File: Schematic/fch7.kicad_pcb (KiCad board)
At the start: 2 copper layers, 30 x 30 mm, 154 parts, among them IC1 MP9943AGQ-Z, IC2 MP9943AGQ-Z, IC3 STM32H743VIT6, IC4 ICM-42688-P, IC5 MPU-6500, J10 PIN2216, J11 PIN2216, J12 PIN2216, J2 PIN2216, J3 PIN2216, J4 PIN2216, J5 PIN2216, J6 PIN2216, J7 PIN2216, J8 PIN2216, J9 PIN2216, SW1 TS24CA, SW2 TS24CA, U1 ME6217C33M5G, U10 HDGC1002WR-S-4P, U11 HDGC1002WR-S-4P, U12 ESP-01F-2M, U13 E28-2G4M27SX, U14 HDGC1002WR-S-4P, U15 HDGC1002WR-S-6P, U16 HDGC1002WR-S-8P, U17 HDGC1002WR-S-8P, U2 ME6217C33M5G, U3 LDO-1.8v, U4 QMC5883L, U5 SPL06-001, U6 CSNP1GCR01-BOW, U7 HDGC1002WR-S-4P, U8 HDGC1002WR-S-4P, U9 HDGC1002WR-S-4P, Y1 8MHz

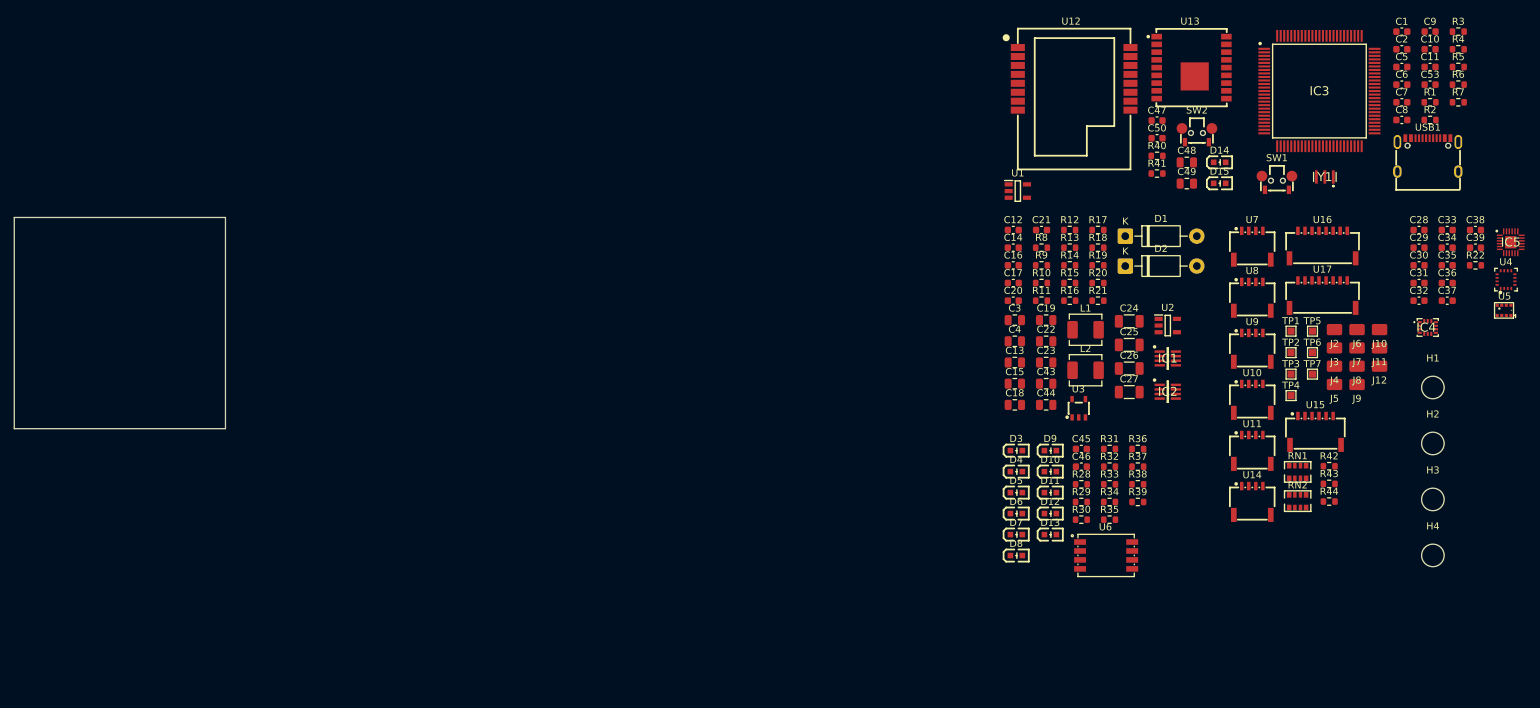
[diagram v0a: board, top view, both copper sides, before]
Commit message: Refactor mounting hole footprints and update schematic
- Deleted obsolete mounting hole footprints from the PCB design.
- Introduced a new footprint "MountingHole_quad_30.5x30.5" for improved layout.
- Updated references in the schematic to use the new mounting hole footprint.
- Adjusted positions of mounting hole symbols in the schematic for better alignment.
- Changed pin types for USB VBUS connections from "power_out" to "bidirectional" for accurate functionality.
- Cleaned up the footprint information cache to reflect the new footprint changes.
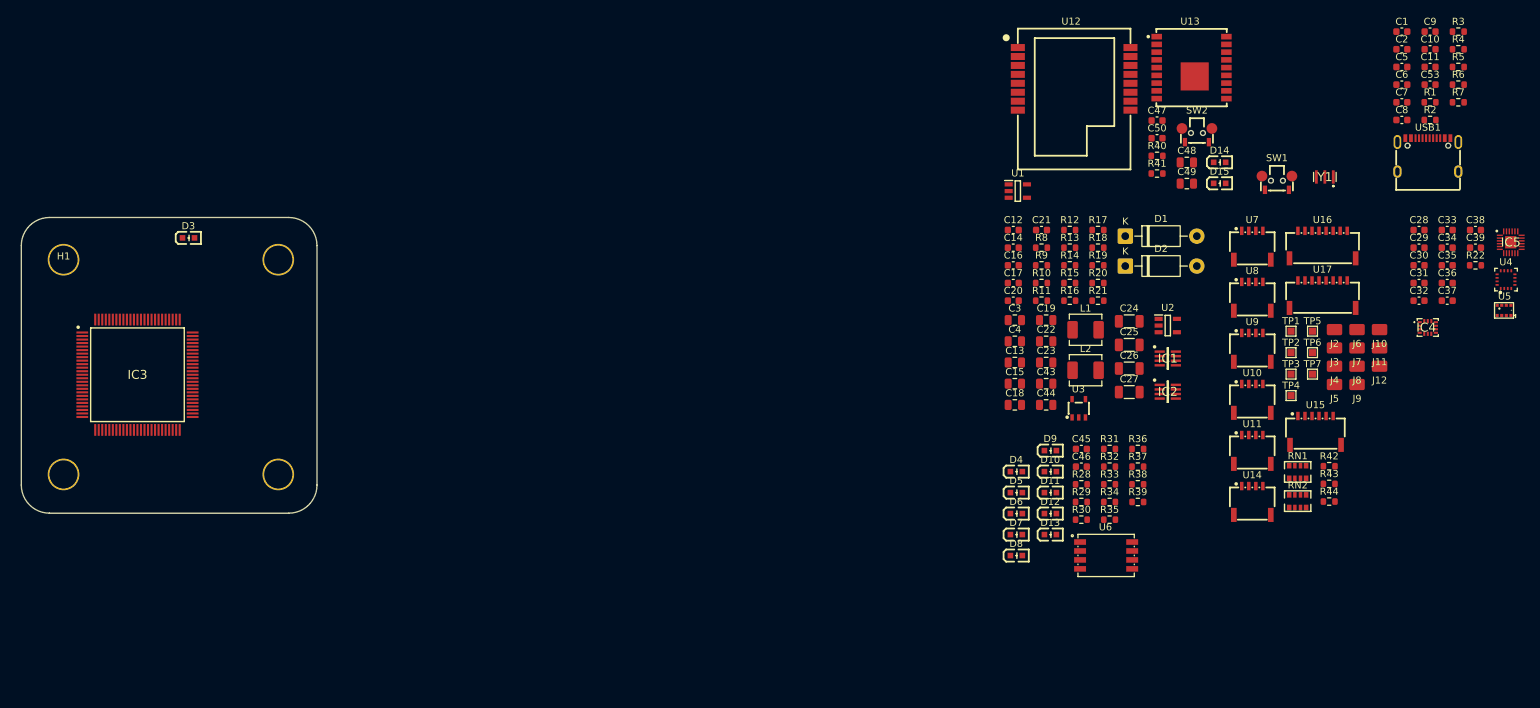
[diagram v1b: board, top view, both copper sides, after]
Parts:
- removed H2, H3, H4: MountingHole, MountingHole:MountingHole_3.2mm_M3
- H1: footprint MountingHole:MountingHole_3.2mm_M3 -> fch7_fp:MountingHole_quad_30.5x30.5
- moved H1 195.3 mm to (69.0, 66.0)
- moved IC3 172.7 mm to (79.5, 82.3)
- moved D3 121.4 mm to (86.8, 62.9)
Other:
- board size 30 x 30 mm -> 42 x 42 mm

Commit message: Update component properties for RF receiver schematic
- Changed the "Value" and "MPN" properties of components in the rf_rx.kicad_sch file from "E28-2G4M27SX" to "ESP-01F-2M".
- Reversed the previous changes for the same properties, updating them back to "E28-2G4M27SX".
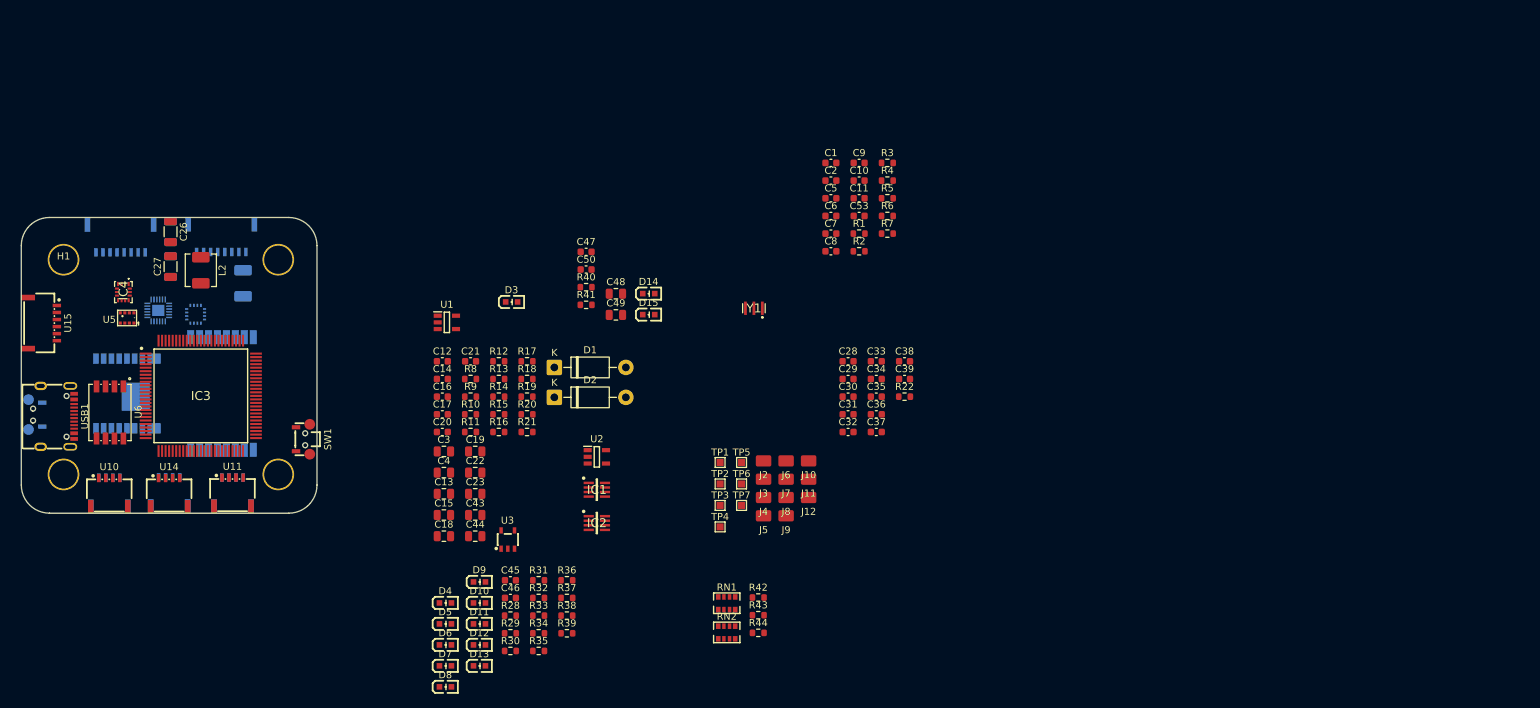
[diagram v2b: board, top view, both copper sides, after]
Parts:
- C24, C25, IC5, L1, SW2, U16, U17, U4, U7, U8, U9: moved to B.Cu
- U12: value ESP-01F-2M -> E28-2G4M27SX; moved to B.Cu
- U13: value E28-2G4M27SX -> ESP-01F-2M; moved to B.Cu
- moved USB1 198.2 mm to (68.1, 88.2), turned to -90 degrees
- moved U5 195.6 mm to (78.0, 74.3)
- moved IC5 192.3 mm to (82.5, 73.2), turned to -90 degrees
- moved U4 186.2 mm to (87.8, 73.8), turned to 180 degrees
- moved IC4 185.3 mm to (77.5, 70.6), turned to -90 degrees
- moved U15 181.5 mm to (66.0, 75.0), turned to -90 degrees
- moved U16 170.7 mm to (77.1, 63.0)
- moved SW2 169.7 mm to (65.0, 88.0), turned to -90 degrees
- moved U9 163.6 mm to (75.5, 99.0), turned to 180 degrees
- moved U10 162.9 mm to (75.5, 99.0)
- moved U13 158.1 mm to (78.0, 85.0), turned to -90 degrees
- moved U17 156.6 mm to (91.4, 63.0)
- moved U8 156.3 mm to (84.0, 99.0), turned to 180 degrees
- moved U14 153.9 mm to (84.0, 99.0)
- moved U7 149.0 mm to (93.0, 99.0), turned to 180 degrees
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
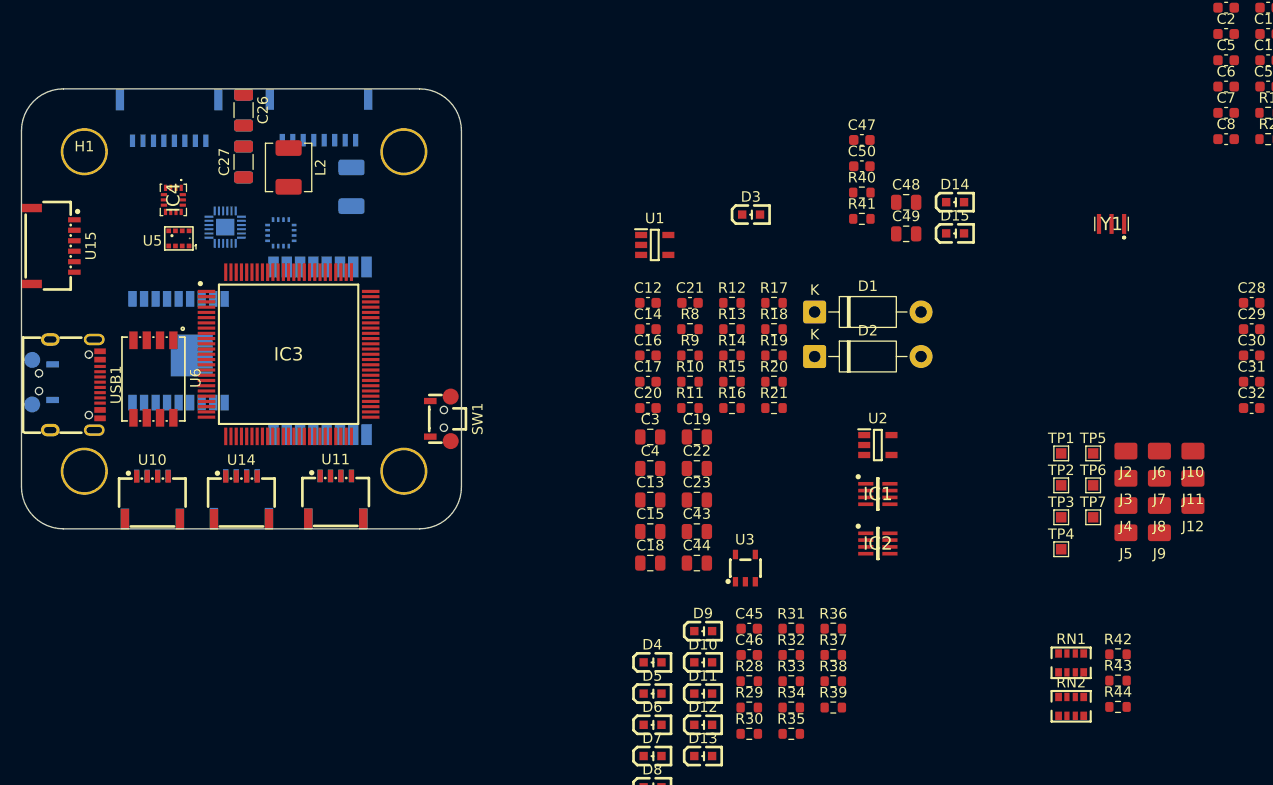
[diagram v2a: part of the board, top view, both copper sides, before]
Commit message: Update fp-info-cache with new component values and add SOD-123 and SOD-323 footprints
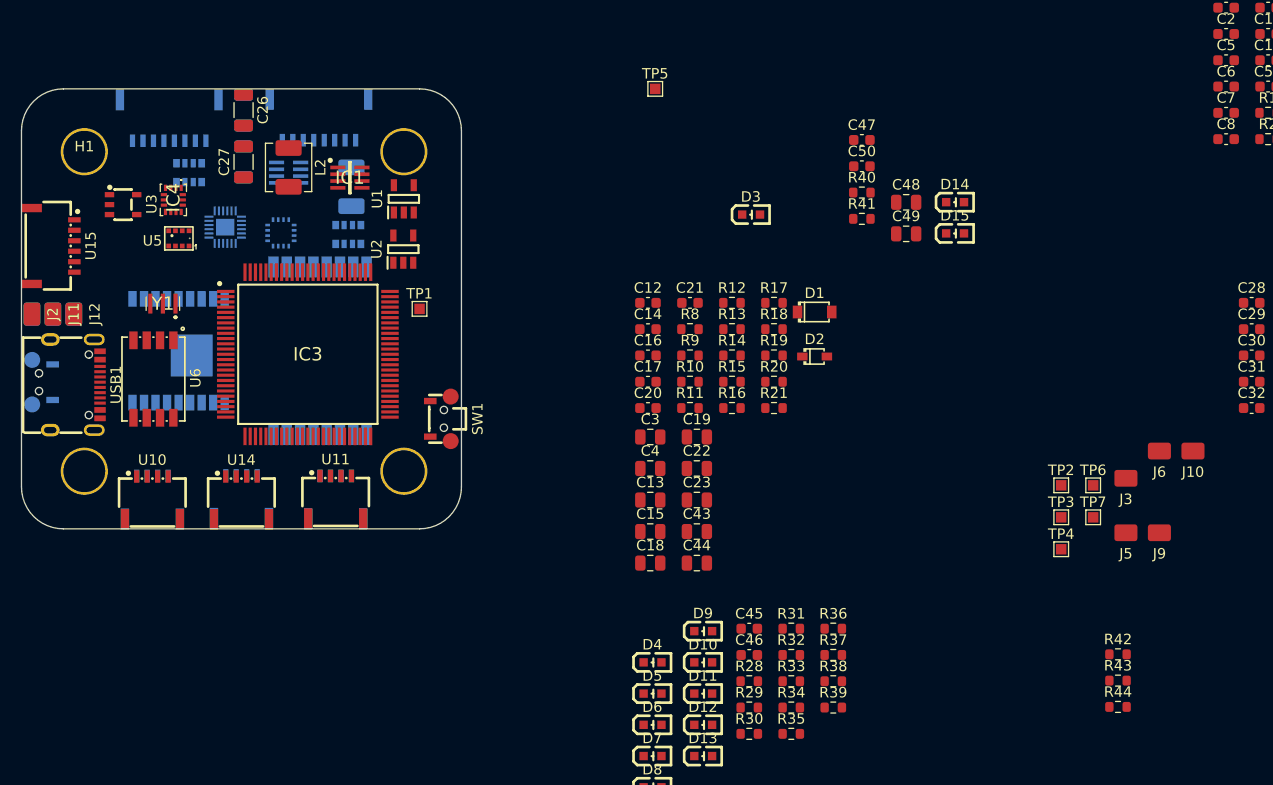
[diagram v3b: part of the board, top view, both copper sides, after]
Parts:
- D1: value 1N5819 -> 1N5819W; footprint Diode_THT:D_DO-41_SOD81_P10.16mm_Horizontal -> fch7_fp:SOD-123_L2.7-W1.6-LS3.7-RD
- D2: value 1N5819 -> BAT60B; footprint Diode_THT:D_DO-41_SOD81_P10.16mm_Horizontal -> fch7_fp:SOD-323_L1.8-W1.3-LS2.5-RD
- IC2, J4, J7, J8, RN1, RN2: moved to B.Cu
- moved J11 110.0 mm to (66.0, 81.5), turned to 90 degrees
- moved J7 108.8 mm to (64.0, 81.5), turned to 90 degrees
- moved J12 108.4 mm to (68.0, 81.5), turned to 90 degrees
- moved J8 107.2 mm to (66.0, 81.5), turned to 90 degrees
- moved J2 105.2 mm to (64.0, 81.5), turned to 90 degrees
- moved J4 102.1 mm to (68.0, 81.5), turned to 90 degrees
- moved RN1 96.3 mm to (79.0, 68.0), turned to 180 degrees
- moved Y1 90.9 mm to (76.5, 80.5)
- moved RN2 82.4 mm to (94.2, 73.9), turned to 180 degrees
- moved U3 68.8 mm to (72.7, 71.0), turned to -90 degrees
- moved IC2 66.5 mm to (88.5, 68.0), turned to 180 degrees
- moved TP1 62.8 mm to (101.0, 81.0)
- moved IC1 58.8 mm to (94.3, 68.5)
- moved TP5 54.4 mm to (123.5, 60.0)
- moved U2 49.0 mm to (99.5, 75.3), turned to 90 degrees
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
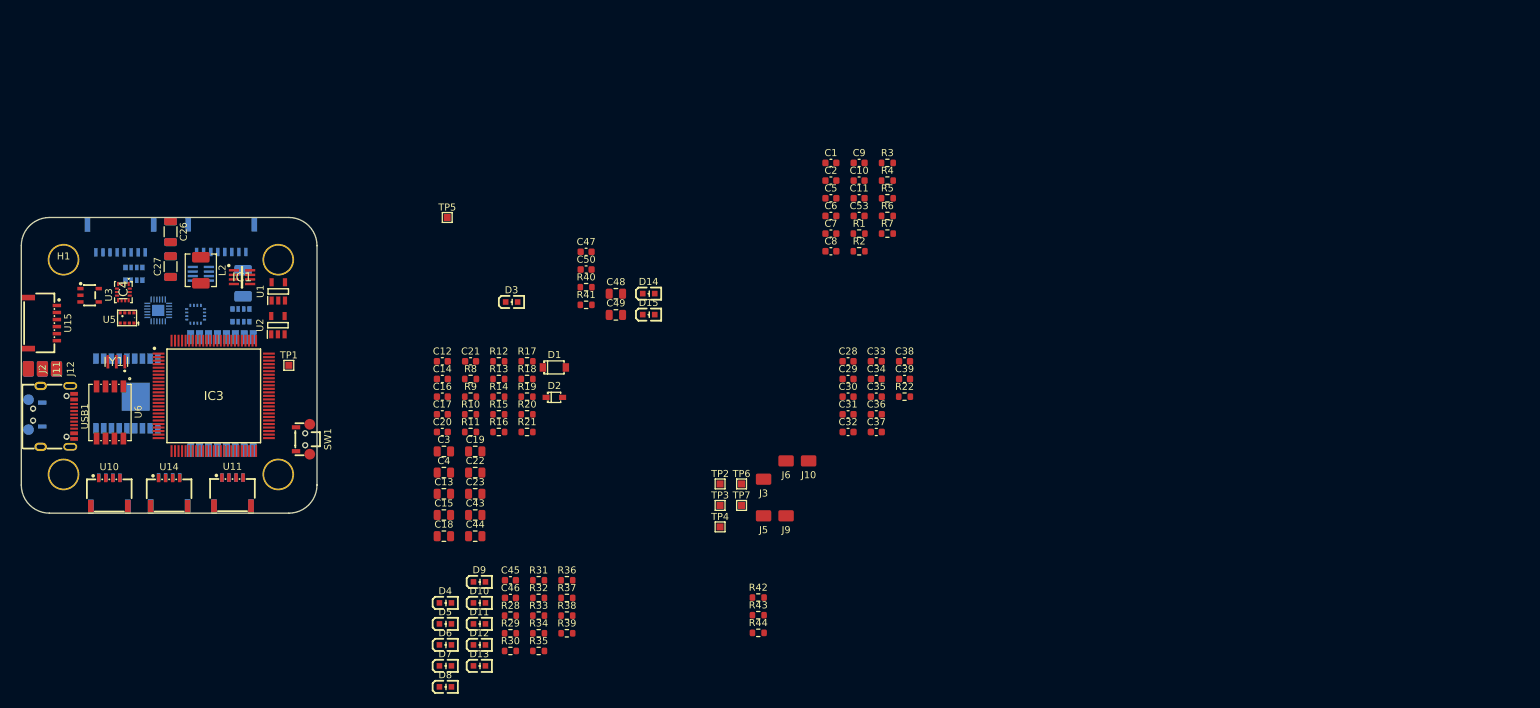
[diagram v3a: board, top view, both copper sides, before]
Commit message: place every big component on pcb
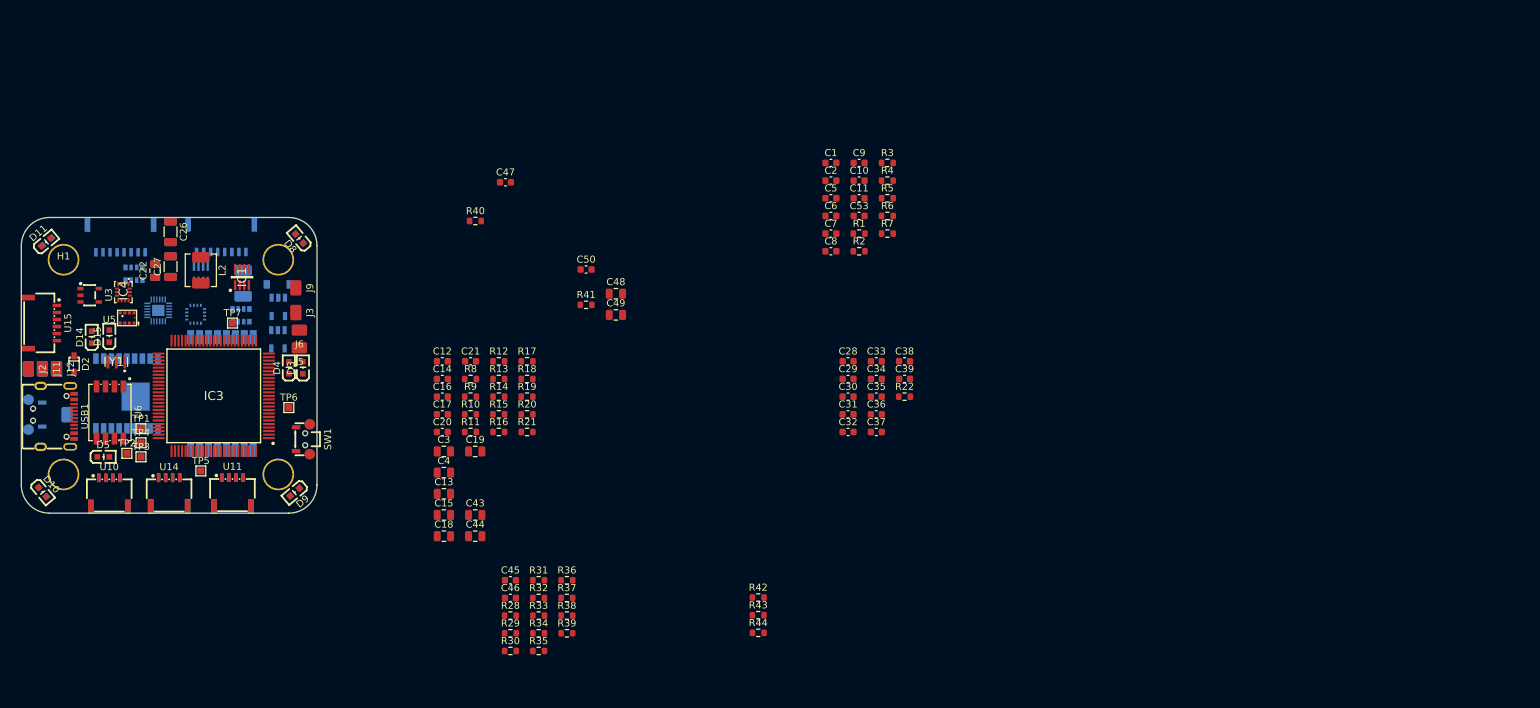
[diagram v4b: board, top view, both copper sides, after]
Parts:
- C23, D1, D12, D13, D6, D7, J10, U1, U2: moved to B.Cu
- moved J10 105.5 mm to (69.5, 88.0), turned to -90 degrees
- moved TP2 84.4 mm to (78.0, 93.5)
- moved TP4 83.1 mm to (80.0, 92.0)
- moved TP3 82.5 mm to (80.0, 94.0)
- moved D11 82.1 mm to (66.5, 63.5), turned to 40 degrees
- moved D6 80.5 mm to (66.7, 63.5), turned to 40 degrees
- moved D14 79.4 mm to (73.0, 77.0), turned to 90 degrees
- moved TP7 76.8 mm to (93.0, 75.0)
- moved J9 76.8 mm to (102.0, 70.0), turned to 90 degrees
- moved D15 76.7 mm to (75.5, 76.9), turned to 90 degrees
- moved J6 71.6 mm to (102.5, 76.0)
- moved J3 70.5 mm to (102.0, 73.5), turned to 90 degrees
- moved J5 70.1 mm to (102.5, 78.5)
- moved D2 68.4 mm to (70.5, 80.8), turned to -90 degrees
- moved D8 67.0 mm to (102.5, 63.0), turned to 130 degrees
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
